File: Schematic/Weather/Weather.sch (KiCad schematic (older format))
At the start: 0 parts

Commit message: More Board Data
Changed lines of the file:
@@
 EESchema Schematic File Version 4
+LIBS:Weather-cache
 EELAYER 29 0
 EELAYER END
 $Descr A4 11693 8268
 encoding utf-8
-Sheet 1 7
+Sheet 1 10
 Title ""
 Date ""
@@
 $EndSheet
 $Sheet
-S 3000 3000 1200 1000
+S 3000 3000 1200 2550
 U 5C96824E
 F0 "Anenometer Control Board" 50
@@
 F3 "J6_P2" I L 3000 3400 50
 F4 "J6_P3" I L 3000 3600 50
+F5 "J7_P1" I R 4200 3200 50
+F6 "J7_P2" I R 4200 3400 50
+F7 "J7_P3" I R 4200 3600 50
+F8 "J7_P4" I R 4200 3800 50
+F9 "J13_P1" I L 3000 4200 50
+F10 "J13_P2" I L 3000 4300 50
+F11 "J13_P3" I L 3000 4400 50
+F12 "J13_P4" I L 3000 4500 50
+F13 "J13_P5" I L 3000 4600 50
+F14 "J13_P6" I L 3000 4700 50
+F15 "J13_P7" I L 3000 4800 50
+F16 "J13_P8" I L 3000 4900 50
 $EndSheet
 Wire Wire Line
@@
 	2500 3600 3000 3600
 $Sheet
-S 3000 4500 1150 850
-U 5C96914D
+S 5000 3000 1500 1750
+U 5C93D4CF
 F0 "External ESP8266" 50
 F1 "Ext_MCU.sch" 50
+F2 "J8_P1" I L 5000 3200 50
+F3 "J8_P2" I L 5000 3400 50
+F4 "J8_P3" I L 5000 3600 50
+F5 "J8_P4" I L 5000 3800 50
+F6 "J9_P1" I R 6500 3150 50
+F7 "J9_P2" I R 6500 3300 50
+F8 "J9_P3" I R 6500 3450 50
+F9 "J9_P4" I R 6500 3600 50
+F10 "J10_P1" I R 6500 4150 50
+F11 "J10_p2" I R 6500 4300 50
+F12 "J10_P3" I R 6500 4450 50
+F13 "J10_P4" I R 6500 4600 50
 $EndSheet
+Wire Wire Line
+	4200 3200 5000 3200
+Wire Wire Line
+	4200 3400 5000 3400
+Wire Wire Line
+	4200 3600 5000 3600
+Wire Wire Line
+	4200 3800 5000 3800
+$Sheet
+S 7500 2500 1350 1250
+U 5C93F504
+F0 "Rain Fall Sensor" 50
+F1 "Rain.sch" 50
+F2 "J11_P1" I L 7500 3150 50
+F3 "J11_P2" I L 7500 3300 50
+F4 "J11_P3" I L 7500 3450 50
+F5 "J11_P4" I L 7500 3600 50
+$EndSheet
+$Sheet
+S 7500 4000 1350 1350
+U 5C93F792
+F0 "Extermal Temp/Hum" 50
+F1 "Sensor2.sch" 50
+F2 "J12_P1" I L 7500 4150 50
+F3 "J12_P2" I L 7500 4300 50
+F4 "J12_P3" I L 7500 4450 50
+F5 "J12_P4" I L 7500 4600 50
+$EndSheet
+Wire Wire Line
+	6500 3150 7500 3150
+Wire Wire Line
+	6500 3300 7500 3300
+Wire Wire Line
+	6500 3450 7500 3450
+Wire Wire Line
+	6500 3600 7500 3600
+Wire Wire Line
+	6500 4150 7500 4150
+Wire Wire Line
+	6500 4300 7500 4300
+Wire Wire Line
+	6500 4450 7500 4450
+Wire Wire Line
+	6500 4600 7500 4600
+$Sheet
+S 1700 4150 800  800
+U 5C952539
+F0 "North Sensor" 50
+F1 "N_Sen.sch" 50
+F2 "J17_P1" I R 2500 4200 50
+F3 "J17_P2" I R 2500 4300 50
+F4 "J17_P3" I R 2500 4400 50
+F5 "J17_P4" I R 2500 4500 50
+F6 "J17_P5" I R 2500 4600 50
+F7 "J17_P6" I R 2500 4700 50
+F8 "J17_P7" I R 2500 4800 50
+F9 "J17_P8" I R 2500 4900 50
+$EndSheet
+Wire Wire Line
+	2500 4200 3000 4200
+Wire Wire Line
+	2500 4300 3000 4300
+Wire Wire Line
+	2500 4400 3000 4400
+Wire Wire Line
+	2500 4500 3000 4500
+Wire Wire Line
+	2500 4600 3000 4600
+Wire Wire Line
+	2500 4700 3000 4700
+Wire Wire Line
+	2500 4800 3000 4800
+Wire Wire Line
+	2500 4900 3000 4900
 $EndSCHEMATC

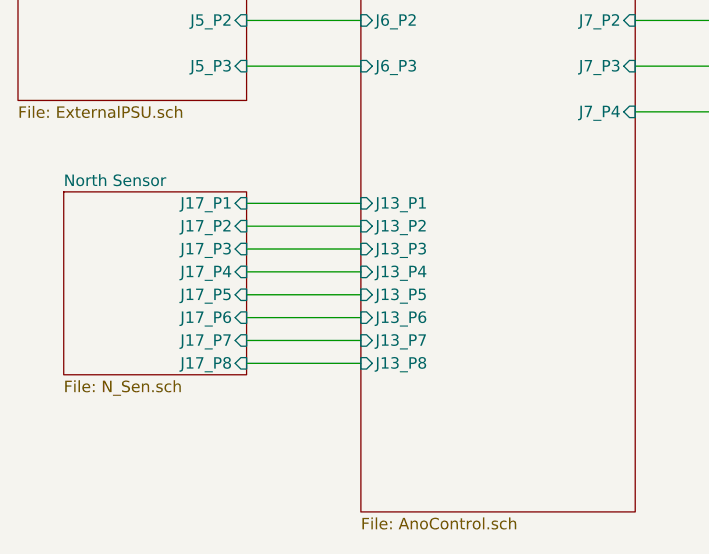
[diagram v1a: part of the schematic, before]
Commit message: Borad layout 2x for Tx Rx
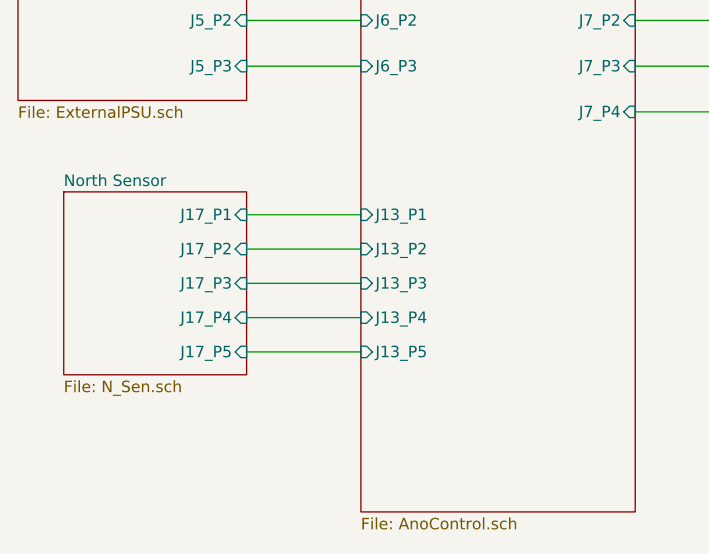
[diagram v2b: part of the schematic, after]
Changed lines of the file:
@@
 F7 "J7_P3" I R 4200 3600 50
 F8 "J7_P4" I R 4200 3800 50
-F9 "J13_P1" I L 3000 4200 50
-F10 "J13_P2" I L 3000 4300 50
-F11 "J13_P3" I L 3000 4400 50
-F12 "J13_P4" I L 3000 4500 50
-F13 "J13_P5" I L 3000 4600 50
-F14 "J13_P6" I L 3000 4700 50
-F15 "J13_P7" I L 3000 4800 50
-F16 "J13_P8" I L 3000 4900 50
+F9 "J13_P1" I L 3000 4250 50
+F10 "J13_P2" I L 3000 4400 50
+F11 "J13_P3" I L 3000 4550 50
+F12 "J13_P4" I L 3000 4700 50
+F13 "J13_P5" I L 3000 4850 50
 $EndSheet
 Wire Wire Line
@@
 Wire Wire Line
 	6500 4600 7500 4600
+Wire Wire Line
+	2500 4250 3000 4250
+Wire Wire Line
+	2500 4550 3000 4550
+Wire Wire Line
+	2500 4400 3000 4400
+Wire Wire Line
+	2500 4700 3000 4700
+Wire Wire Line
+	2500 4850 3000 4850
 $Sheet
 S 1700 4150 800  800
@@
 F0 "North Sensor" 50
 F1 "N_Sen.sch" 50
-F2 "J17_P1" I R 2500 4200 50
-F3 "J17_P2" I R 2500 4300 50
-F4 "J17_P3" I R 2500 4400 50
-F5 "J17_P4" I R 2500 4500 50
-F6 "J17_P5" I R 2500 4600 50
-F7 "J17_P6" I R 2500 4700 50
-F8 "J17_P7" I R 2500 4800 50
-F9 "J17_P8" I R 2500 4900 50
+F2 "J17_P1" I R 2500 4250 50
+F3 "J17_P2" I R 2500 4400 50
+F4 "J17_P3" I R 2500 4550 50
+F5 "J17_P4" I R 2500 4700 50
+F6 "J17_P5" I R 2500 4850 50
 $EndSheet
-Wire Wire Line
-	2500 4200 3000 4200
-Wire Wire Line
-	2500 4300 3000 4300
-Wire Wire Line
-	2500 4400 3000 4400
-Wire Wire Line
-	2500 4500 3000 4500
-Wire Wire Line
-	2500 4600 3000 4600
-Wire Wire Line
-	2500 4700 3000 4700
-Wire Wire Line
-	2500 4800 3000 4800
-Wire Wire Line
-	2500 4900 3000 4900
 $EndSCHEMATC

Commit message: more board layouts
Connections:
- wire segments 26 -> 31
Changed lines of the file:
@@
 $Descr A4 11693 8268
 encoding utf-8
-Sheet 1 10
+Sheet 1 11
 Title ""
 Date ""
@@
 F3 "J5_P2" I R 2500 3400 50
 F4 "J5_P3" I R 2500 3600 50
-$EndSheet
-$Sheet
-S 3000 3000 1200 2550
-U 5C96824E
-F0 "Anenometer Control Board" 50
-F1 "AnoControl.sch" 50
-F2 "J6_P1" I L 3000 3200 50
-F3 "J6_P2" I L 3000 3400 50
-F4 "J6_P3" I L 3000 3600 50
-F5 "J7_P1" I R 4200 3200 50
-F6 "J7_P2" I R 4200 3400 50
-F7 "J7_P3" I R 4200 3600 50
-F8 "J7_P4" I R 4200 3800 50
-F9 "J13_P1" I L 3000 4250 50
-F10 "J13_P2" I L 3000 4400 50
-F11 "J13_P3" I L 3000 4550 50
-F12 "J13_P4" I L 3000 4700 50
-F13 "J13_P5" I L 3000 4850 50
 $EndSheet
 Wire Wire Line
@@
 	6500 4600 7500 4600
 Wire Wire Line
-	2500 4250 3000 4250
+	2450 4250 2950 4250
 Wire Wire Line
-	2500 4550 3000 4550
+	2450 4550 2950 4550
 Wire Wire Line
-	2500 4400 3000 4400
+	2450 4400 2950 4400
 Wire Wire Line
-	2500 4700 3000 4700
+	2450 4700 2950 4700
 Wire Wire Line
-	2500 4850 3000 4850
+	2450 4850 2950 4850
 $Sheet
-S 1700 4150 800  800
+S 1650 4150 800  800
 U 5C952539
 F0 "North Sensor" 50
 F1 "N_Sen.sch" 50
-F2 "J17_P1" I R 2500 4250 50
-F3 "J17_P2" I R 2500 4400 50
-F4 "J17_P3" I R 2500 4550 50
-F5 "J17_P4" I R 2500 4700 50
-F6 "J17_P5" I R 2500 4850 50
+F2 "J17_P1" I R 2450 4250 50
+F3 "J17_P2" I R 2450 4400 50
+F4 "J17_P3" I R 2450 4550 50
+F5 "J17_P4" I R 2450 4700 50
+F6 "J17_P5" I R 2450 4850 50
 $EndSheet
+$Sheet
+S 1650 5400 800  800
+U 5C9F4D88
+F0 "South Sensor" 50
+F1 "S_Sen.sch" 50
+F2 "J18_P1" I R 2450 5500 50
+F3 "J18_P2" I R 2450 5650 50
+F4 "J18_P3" I R 2450 5800 50
+F5 "J18_P4" I R 2450 5950 50
+F6 "J18_P5" I R 2450 6100 50
+$EndSheet
+$Sheet
+S 2950 2950 1300 4500
+U 5C96824E
+F0 "Anenometer Control Board" 50
+F1 "AnoControl.sch" 50
+F2 "J6_P1" I L 2950 3150 50
+F3 "J6_P2" I L 2950 3350 50
+F4 "J6_P3" I L 2950 3550 50
+F5 "J7_P1" I R 4250 3150 50
+F6 "J7_P2" I R 4250 3350 50
+F7 "J7_P3" I R 4250 3550 50
+F8 "J7_P4" I R 4250 3750 50
+F9 "J13_P1" I L 2950 4200 50
+F10 "J13_P2" I L 2950 4350 50
+F11 "J13_P3" I L 2950 4500 50
+F12 "J13_P4" I L 2950 4650 50
+F13 "J13_P5" I L 2950 4800 50
+F14 "J14_P1" I L 2950 5500 50
+F15 "J14_P2" I L 2950 5650 50
+F16 "J14_P3" I L 2950 5800 50
+F17 "J14_P4" I L 2950 5950 50
+F18 "J14_P5" I L 2950 6100 50
+$EndSheet
+Wire Wire Line
+	2450 5500 2950 5500
+Wire Wire Line
+	2450 5650 2950 5650
+Wire Wire Line
+	2450 5800 2950 5800
+Wire Wire Line
+	2450 5950 2950 5950
+Wire Wire Line
+	2450 6100 2950 6100
 $EndSCHEMATC

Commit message: More boards added
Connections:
- wire segments 31 -> 41
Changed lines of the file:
@@
 $Descr A4 11693 8268
 encoding utf-8
-Sheet 1 11
+Sheet 1 13
 Title ""
 Date ""
@@
 F17 "J14_P4" I L 2950 5950 50
 F18 "J14_P5" I L 2950 6100 50
+F19 "J21_P1" I R 4250 5500 50
+F20 "J21_P2" I R 4250 5650 50
+F21 "J21_P3" I R 4250 5800 50
+F22 "J21_P4" I R 4250 5950 50
+F23 "J21_P5" I R 4250 6100 50
+F24 "J22_P1" I R 4250 6700 50
+F25 "J22_P2" I R 4250 6850 50
+F26 "J22_P3" I R 4250 7000 50
+F27 "J22_P4" I R 4250 7150 50
+F28 "J22_P5" I R 4250 7300 50
 $EndSheet
 Wire Wire Line
@@
 Wire Wire Line
 	2450 6100 2950 6100
+$Sheet
+S 5000 5400 900  800
+U 5CAC04D1
+F0 "Eath Sensor" 50
+F1 "E_Sen.sch" 50
+F2 "J19_P1" I L 5000 5500 50
+F3 "J19_P2" I L 5000 5650 50
+F4 "J19_P3" I L 5000 5800 50
+F5 "J19_P4" I L 5000 5950 50
+F6 "J19_P5" I L 5000 6100 50
+$EndSheet
+$Sheet
+S 5000 6550 900  850
+U 5CAC05F6
+F0 "West Sensor" 50
+F1 "W_Sen.sch" 50
+F2 "J20_P1" I L 5000 6700 50
+F3 "J20_P2" I L 5000 6850 50
+F4 "J20_P3" I L 5000 7000 50
+F5 "J20_P4" I L 5000 7150 50
+F6 "J20_P5" I L 5000 7300 50
+$EndSheet
+Wire Wire Line
+	4250 5500 5000 5500
+Wire Wire Line
+	4250 5650 5000 5650
+Wire Wire Line
+	4250 5800 5000 5800
+Wire Wire Line
+	4250 5950 5000 5950
+Wire Wire Line
+	4250 6100 5000 6100
+Wire Wire Line
+	4250 6700 5000 6700
+Wire Wire Line
+	4250 6850 5000 6850
+Wire Wire Line
+	4250 7000 5000 7000
+Wire Wire Line
+	4250 7150 5000 7150
+Wire Wire Line
+	4250 7300 5000 7300
 $EndSCHEMATC

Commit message: new M_Board internal
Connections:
- wire segments 41 -> 35
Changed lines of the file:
@@
 $Descr A4 11693 8268
 encoding utf-8
-Sheet 1 13
+Sheet 1 14
 Title ""
 Date ""
@@
 $EndSheet
 $Sheet
-S 3000 1350 750  550
+S 4400 2100 750  550
 U 5C9253D5
 F0 "Internal ESP8266" 50
 F1 "Int_MCU.sch" 50
-F2 "J2_P1" I L 3000 1450 50
-F3 "J2_P2" I L 3000 1600 50
-F4 "J3_P1" I R 3750 1500 50
-F5 "J3_P2" I R 3750 1600 50
-F6 "J3_P3" I R 3750 1700 50
-F7 "J3_P4" I R 3750 1800 50
+F2 "J2_P1" I L 4400 2200 50
+F3 "J2_P2" I L 4400 2350 50
+F4 "J3_P1" I R 5150 2250 50
+F5 "J3_P2" I R 5150 2350 50
+F6 "J3_P3" I R 5150 2450 50
+F7 "J3_P4" I R 5150 2550 50
 $EndSheet
 $Sheet
@@
 F5 "J4_P4" I L 4400 1800 50
 $EndSheet
-Wire Wire Line
-	2400 1450 3000 1450
-Wire Wire Line
-	2400 1600 3000 1600
-Wire Wire Line
-	3750 1500 4400 1500
-Wire Wire Line
-	3750 1600 4400 1600
-Wire Wire Line
-	3750 1700 4400 1700
-Wire Wire Line
-	3750 1800 4400 1800
 $Sheet
 S 1500 3000 1000 750
@@
 Wire Wire Line
 	4250 7300 5000 7300
+$Sheet
+S 3000 1500 750  1000
+U 5CAF7F5D
+F0 "Int Motherboard" 50
+F1 "Int_M_Board.sch" 50
+$EndSheet
 $EndSCHEMATC

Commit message: more changes
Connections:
- wire segments 35 -> 37
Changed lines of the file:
@@
 $Descr A4 11693 8268
 encoding utf-8
-Sheet 1 14
+Sheet 1 15
 Title ""
 Date ""
@@
 $EndDescr
 $Sheet
-S 1500 1350 900  350
+S 1200 800  900  350
 U 5C9252D8
 F0 "PSU 1" 50
 F1 "internalPSU.sch" 50
-F2 "J1_P1" I R 2400 1450 50
-F3 "J1_P2" I R 2400 1600 50
-$EndSheet
-$Sheet
-S 4400 2100 750  550
+F2 "J1_P1" I R 2100 900 50
+F3 "J1_P2" I R 2100 1050 50
+$EndSheet
+$Sheet
+S 1400 1450 700  750
 U 5C9253D5
 F0 "Internal ESP8266" 50
 F1 "Int_MCU.sch" 50
-F2 "J2_P1" I L 4400 2200 50
-F3 "J2_P2" I L 4400 2350 50
-F4 "J3_P1" I R 5150 2250 50
-F5 "J3_P2" I R 5150 2350 50
-F6 "J3_P3" I R 5150 2450 50
-F7 "J3_P4" I R 5150 2550 50
-$EndSheet
-$Sheet
-S 4400 1350 700  550
+F2 "J3_P1" I L 1400 1600 50
+F3 "J3_P2" I L 1400 1700 50
+F4 "J3_P3" I L 1400 1800 50
+F5 "J3_P4" I L 1400 1900 50
+F6 "J3_P6" I L 1400 2100 50
+F7 "J3_P5" I L 1400 2000 50
+$EndSheet
+$Sheet
+S 4100 650  700  550
 U 5C9254A0
-F0 "Internal Sensors" 50
+F0 "Internal Temp/Hum" 50
 F1 "Sensor1.sch" 50
-F2 "J4_P1" I L 4400 1500 50
-F3 "J4_P2" I L 4400 1600 50
-F4 "J4_P3" I L 4400 1700 50
-F5 "J4_P4" I L 4400 1800 50
+F2 "J4_P1" I L 4100 800 50
+F3 "J4_P2" I L 4100 900 50
+F4 "J4_P3" I L 4100 1000 50
+F5 "J4_P4" I L 4100 1100 50
 $EndSheet
 $Sheet
@@
 	4250 7300 5000 7300
 $Sheet
-S 3000 1500 750  1000
+S 2700 800  900  1450
 U 5CAF7F5D
 F0 "Int Motherboard" 50
 F1 "Int_M_Board.sch" 50
+F2 "J2_P1" I L 2700 900 50
+F3 "J2_P2" I L 2700 1050 50
+$EndSheet
+Wire Wire Line
+	2100 900  2700 900
+Wire Wire Line
+	2100 1050 2700 1050
+$Sheet
+S 4100 1500 750  700
+U 5CB297E4
+F0 "Internal Pressure" 50
+F1 "Sensor3.sch" 50
 $EndSheet
 $EndSCHEMATC
